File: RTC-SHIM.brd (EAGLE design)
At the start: 27.9 x 53 mm, 11 parts, among them IC1 DS3231/SO

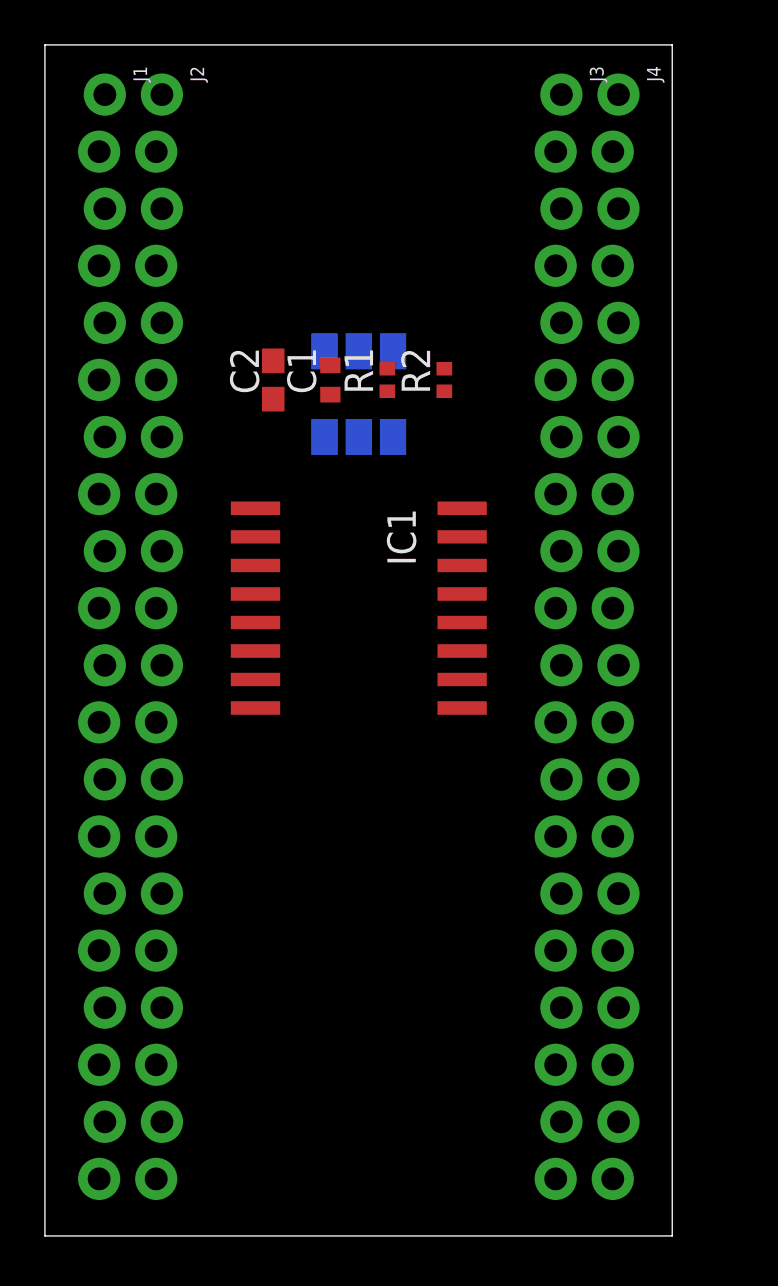
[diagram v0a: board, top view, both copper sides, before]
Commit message: Added Battery holder and some logos and texts.
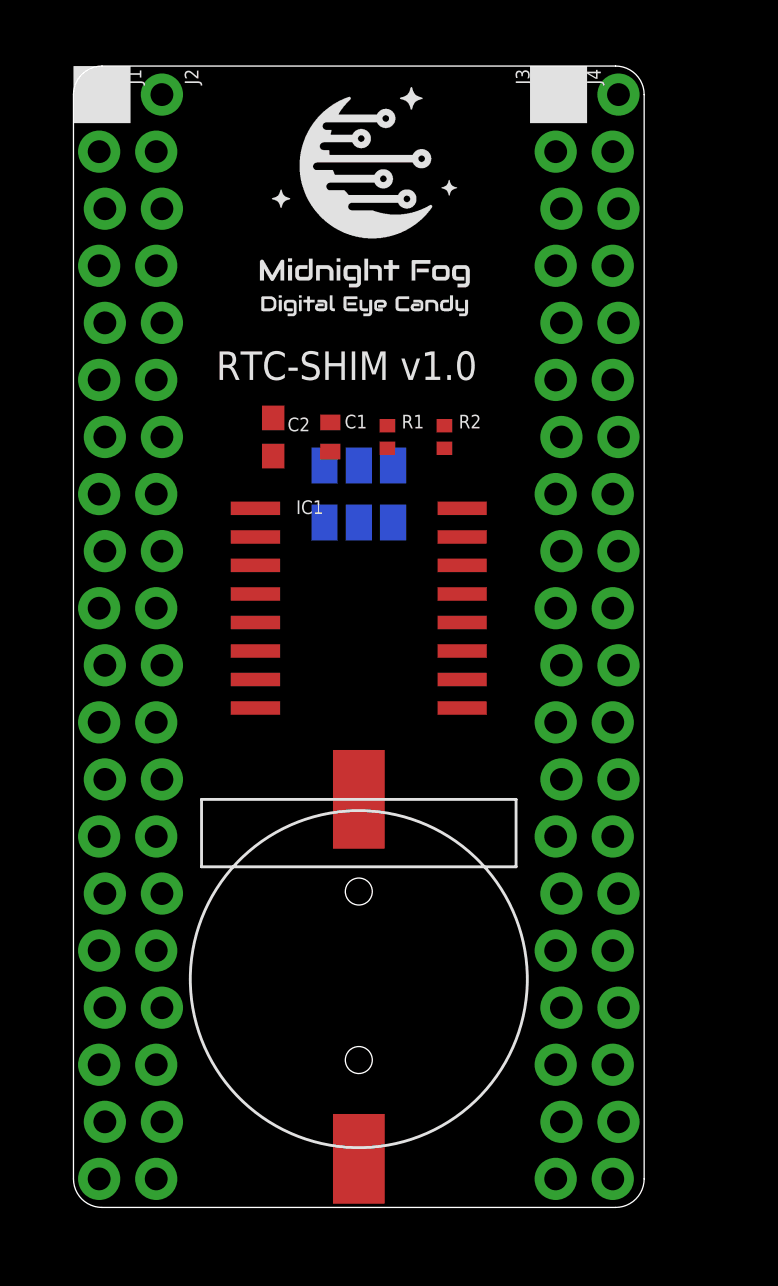
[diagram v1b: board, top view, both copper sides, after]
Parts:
- added BAT1: CR1220-2, CR1220-2:CR1220-2
- added LOGO1: MFDECLOGO_SQ_8MM, _my_logos:MFDEC_SQ_8MM
- added LOGO2: MFDECLOGO_L_20MM, _my_logos:MFDEC_L_20MM
- added LOGO3: RSNURL_QR_10MM, _my_logos:RSNURL_QR_10MM
- moved SJ1 5.08 mm to (14.0, 34.3)
- moved SJ2 3.81 mm to (14.0, 31.8)
- moved C1 2.54 mm to (12.7, 35.6)
- moved C2 2.54 mm to (10.2, 35.6)
- moved R1 2.54 mm to (15.2, 35.6)
- moved R2 2.54 mm to (17.8, 35.6)
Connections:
- net GND: now also BAT1.BAT-
- net VBAT: now also BAT1.BAT+
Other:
- board size 27.9 x 53 mm -> 25.4 x 50.8 mm
- board text added: "I2C bus selection"
- board text added: "I2C0"
- board text added: "I2C1"
- board text added: "RTC-SHIM v1.0"
- board text added: "http://redscorp.net"

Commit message: Moved stuff around a little bit.
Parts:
- moved LOGO1 1.80 mm to (7.62, 39.4)
- moved C1 1.80 mm to (11.4, 34.3)
- moved C2 1.80 mm to (8.89, 34.3)
- moved LOGO3 1.80 mm to (17.8, 39.4)
- moved R1 1.80 mm to (14.0, 34.3)
- moved R2 1.80 mm to (16.5, 34.3)
- moved BAT1 1.80 mm to (12.7, 10.2)
- moved IC1 1.80 mm to (12.7, 26.7)
- moved SJ2 1.80 mm to (12.7, 30.5)
- moved LOGO2 1.80 mm to (-0.25, -5.71)
- moved SJ1 1.80 mm to (12.7, 33.0)
- moved J1 1.80 mm to (1.27, 49.5)
- moved J2 1.80 mm to (3.81, 49.5)
- moved J3 1.80 mm to (21.6, 49.5)
- moved J4 1.80 mm to (24.1, 49.5)

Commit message: Trace the board. Add CAM files.
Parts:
- moved LOGO2 1.14 mm to (-0.25, -4.57)
- moved SJ2 0.25 mm to (12.7, 30.2)
- moved SJ1 0.13 mm to (12.7, 33.1)
- turned R1 to 270 degrees
- turned R2 to 270 degrees
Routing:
- net GND: track 0.00 -> 443.6 mm, vias 0 -> 85
- net 3.3V: track 0.00 -> 74.0 mm, vias 0 -> 4
- net SDA0: track 0.00 -> 44.7 mm, vias 0 -> 3
- net SCL1: track 0.00 -> 44.1 mm, vias 0 -> 3
- net SDA1: track 0.00 -> 42.0 mm, vias 0 -> 3
- net SCL0: track 0.00 -> 41.5 mm, vias 0 -> 3
- net SDA: track 0.00 -> 15.8 mm, vias 0 -> 3
- net VBAT: track 0.00 -> 14.6 mm, vias 0 -> 2
- net SCL: track 0.00 -> 12.8 mm, vias 0 -> 4
- added copper zone on layer 1, net GND
- added copper zone on layer 16, net GND
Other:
- board text added: "(c) Andriy Golovnya"
- board text added: "+"
- board text added: "-"
- board text added: "3V CR1220"

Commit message: Add few texts. Move some traces around. Updated description.
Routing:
- net SCL: track 12.8 -> 11.4 mm, vias 4 -> 3
- net GND: track 443.6 -> 443.7 mm, vias 85 -> 84
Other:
- board text added: "BOTTOM SIDE"
- board text added: "TOP SIDE"

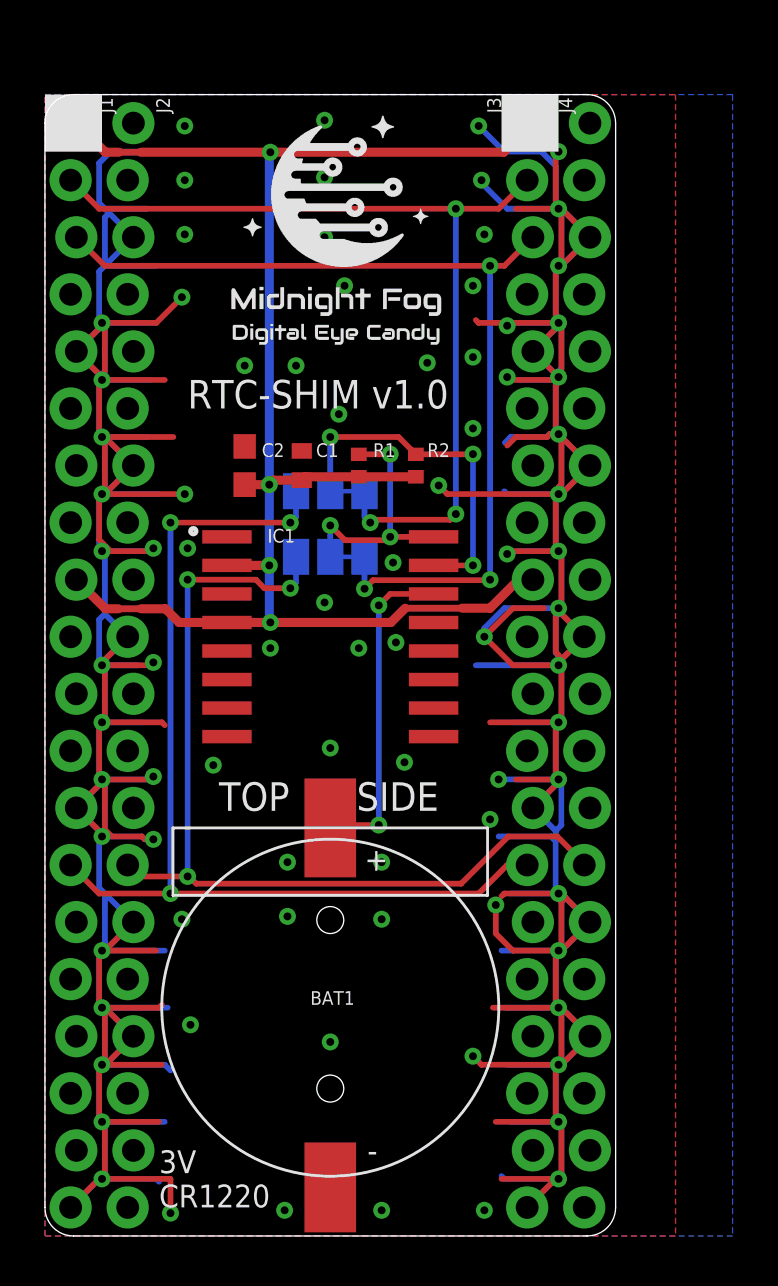
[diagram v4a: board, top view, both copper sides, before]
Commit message: Removed unneeded traces. generated new CAM.
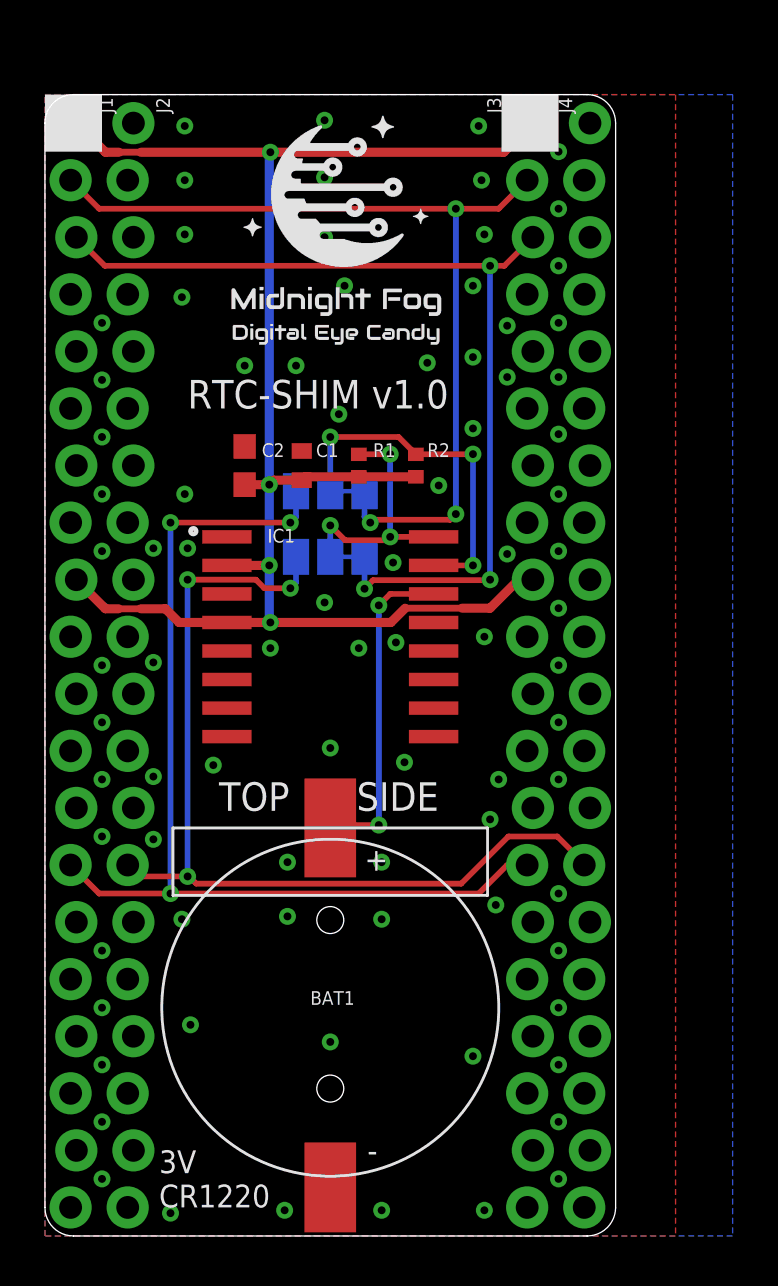
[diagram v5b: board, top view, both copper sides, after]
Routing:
- net GND: track 443.7 -> 2.30 mm

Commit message: Added battery connector. Generated CAM.
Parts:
- added LIPO1: Molex VERT 1.25mm pitch, PiB_connectors:_MOLEX-0530470210_VERT_PITCH-1.25MM
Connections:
- net GND: now also LIPO1.2
- net VBAT: now also LIPO1.1
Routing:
- net VBAT: track 14.6 -> 32.3 mm
- net GND: vias 84 -> 86
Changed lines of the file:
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@@
 <layer number="154" name="FabDoc2" color="2" fill="1" visible="no" active="no"/>
 <layer number="155" name="FabDoc3" color="7" fill="15" visible="no" active="no"/>
+<layer number="160" name="tMountFaceplate" color="7" fill="1" visible="yes" active="yes"/>
+<layer number="161" name="bMountFaceplate" color="7" fill="1" visible="yes" active="yes"/>
+<layer number="162" name="tCopperArt" color="7" fill="1" visible="yes" active="yes"/>
+<layer number="163" name="bCopperArt" color="7" fill="1" visible="yes" active="yes"/>
+<layer number="164" name="tRubout" color="7" fill="1" visible="yes" active="yes"/>
+<layer number="165" name="bRubout" color="7" fill="1" visible="yes" active="yes"/>
+<layer number="167" name="Fiducials" color="7" fill="1" visible="yes" active="yes"/>
+<layer number="169" name="internal" color="7" fill="1" visible="yes" active="yes"/>
 <layer number="199" name="Contour" color="7" fill="1" visible="no" active="yes"/>
 <layer number="200" name="200bmp" color="1" fill="10" visible="no" active="yes"/>
@@
 <element name="LOGO2" library="_my_logos" package="MFDEC_L_20MM" value="MFDECLOGO_L_20MM" x="-0.254" y="-4.572" smashed="yes" rot="MR90"/>
 <element name="LOGO3" library="_my_logos" package="RSNURL_QR_10MM" value="RSNURL_QR_10MM" x="17.78" y="39.37" smashed="yes" rot="MR0"/>
+<element name="LIPO1" library="PiB_connectors" package="_MOLEX-0530470210_VERT_PITCH-1.25MM" package3d_urn="urn:adsk.eagle:package:2973718/3" value="Molex VERT 1.25mm pitch" x="18.161" y="2.286" smashed="yes" rot="R180">
+<attribute name="DATASHEET_CONNECTOR1" value="https://www.molex.com/pdm_docs/sd/530470210_sd.pdf" x="18.161" y="2.286" size="1.778" layer="27" rot="R180" display="off"/>
+<attribute name="DATASHEET_CONNECTOR2" value="https://www.molex.com/pdm_docs/sd/510210700_sd.pdf" x="18.161" y="2.286" size="1.778" layer="27" rot="R180" display="off"/>
+<attribute name="DATASHEET_CRIMP" value="https://www.molex.com/pdm_docs/sd/500798000_sd.pdf" x="18.161" y="2.286" size="1.778" layer="27" rot="R180" display="off"/>
+<attribute name="DISTLINK_CONNECTOR1" value="https://www.digikey.com/products/en?keywords=WM1731-ND" x="18.161" y="2.286" size="1.778" layer="27" rot="R180" display="off"/>
+<attribute name="DISTLINK_CONNECTOR2" value="https://www.digikey.com/products/en?keywords=WM1720-ND" x="18.161" y="2.286" size="1.778" layer="27" rot="R180" display="off"/>
+<attribute name="DISTLINK_CRIMP" value="https://www.digikey.com/products/en?keywords=WM1142CT-ND" x="18.161" y="2.286" size="1.778" layer="27" rot="R180" display="off"/>
+<attribute name="DISTPN_CONNECTOR1" value="WM1731-ND" x="18.161" y="2.286" size="1.778" layer="27" rot="R180" display="off"/>
+<attribute name="DISTPN_CONNECTOR2" value="WM1720-ND" x="18.161" y="2.286" size="1.778" layer="27" rot="R180" display="off"/>
+<attribute name="DISTPN_CRIMP" value="WM1142CT-ND" x="18.161" y="2.286" size="1.778" layer="27" rot="R180" display="off"/>
+<attribute name="DIST_CONNECTOR1" value="Digikey" x="18.161" y="2.286" size="1.778" layer="27" rot="R180" display="off"/>
+<attribute name="DIST_CONNECTOR2" value="Digikey" x="18.161" y="2.286" size="1.778" layer="27" rot="R180" display="off"/>
+<attribute name="DIST_CRIMP" value="Digikey" x="18.161" y="2.286" size="1.778" layer="27" rot="R180" display="off"/>
+<attribute name="MFR_CONNECTOR1" value="Molex, LLC" x="18.161" y="2.286" size="1.778" layer="27" rot="R180" display="off"/>
+<attribute name="MFR_CONNECTOR2" value="Molex, LLC" x="18.161" y="2.286" size="1.778" layer="27" rot="R180" display="off"/>
+<attribute name="MFR_CRIMP" value="Molex, LLC" x="18.161" y="2.286" size="1.778" layer="27" rot="R180" display="off"/>
+<attribute name="MPN_CONNECTOR1" value="0530470210" x="18.161" y="2.286" size="1.778" layer="27" rot="R180" display="off"/>
+<attribute name="MPN_CONNECTOR2" value="51021-0200" x="18.161" y="2.286" size="1.778" layer="27" rot="R180" display="off"/>
+<attribute name="MPN_CRIMP" value="0500798000" x="18.161" y="2.286" size="1.778" layer="27" rot="R180" display="off"/>
+<attribute name="NAME" x="18.034" y="3.81" size="0.6096" layer="25" font="vector"/>
+<attribute name="VALUE" x="18.161" y="1.524" size="0.25" layer="27" font="vector" ratio="10" rot="R180" align="bottom-center"/>
+</element>
 </elements>
 <signals>
@@
 <wire x1="14.859" y1="18.288" x2="12.828" y2="18.288" width="0.254" layer="1"/>
 <wire x1="12.828" y1="18.288" x2="12.7" y2="18.16" width="0.254" layer="1"/>
+<contactref element="LIPO1" pad="1"/>
+<wire x1="14.859" y1="18.288" x2="15.738" y2="17.409" width="0.254" layer="16"/>
+<wire x1="15.738" y1="17.409" x2="15.738" y2="5.588" width="0.254" layer="16"/>
+<wire x1="18.786" y1="2.54" x2="18.786" y2="2.286" width="0.254" layer="16"/>
+<wire x1="18.786" y1="2.54" x2="15.738" y2="5.588" width="0.254" layer="16"/>
 </signal>
 <signal name="SCL">
@@
 <via x="10.795" y="14.224" extent="1-16" drill="0.35"/>
 <via x="6.477" y="9.398" extent="1-16" drill="0.35"/>
-<via x="19.05" y="8.001" extent="1-16" drill="0.35"/>
+<via x="19.05" y="5.588" extent="1-16" drill="0.35"/>
 <wire x1="19.431" y1="46.863" x2="19.431" y2="46.99" width="0.254" layer="16"/>
 <via x="10.033" y="26.162" extent="1-16" drill="0.35"/>
@@
 <via x="11.176" y="38.735" extent="1-16" drill="0.35"/>
 <via x="15.494" y="29.972" extent="1-16" drill="0.35"/>
+<contactref element="LIPO1" pad="2"/>
+<via x="14.986" y="6.477" extent="1-16" drill="0.35"/>
+<via x="17.018" y="10.795" extent="1-16" drill="0.35"/>
 </signal>
 <signal name="SCL0">
